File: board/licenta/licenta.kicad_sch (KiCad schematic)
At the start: 70 parts, among them IC1 SAMACSYS_PARTS_NCP186BMX330TAG, IC3 SAMACSYS_PARTS_BMI085, J1 SAMACSYS_PARTS_USB4110-GF-A, J2 SAMACSYS_PARTS_112A-TAAR-R03_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, J3 Conn_01x07, Q1 ESP32_WROVER_SPARKFUN-DISCRET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, Q2 2N7002, SW1 SELECT, SW2 UP, SW3 DOWN, SW4 RESET, SW5 DOWN, U1 ESP32-C3-MINI-1, U2 ESP32_WROVER_SPARKFUN-IC-POWE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, U3 DRV2605LDGS, U4 GC9A01_IPS_display_SPI, U5 A1027, U6 TPS3831, U7 ESP32-S3-MINI-1

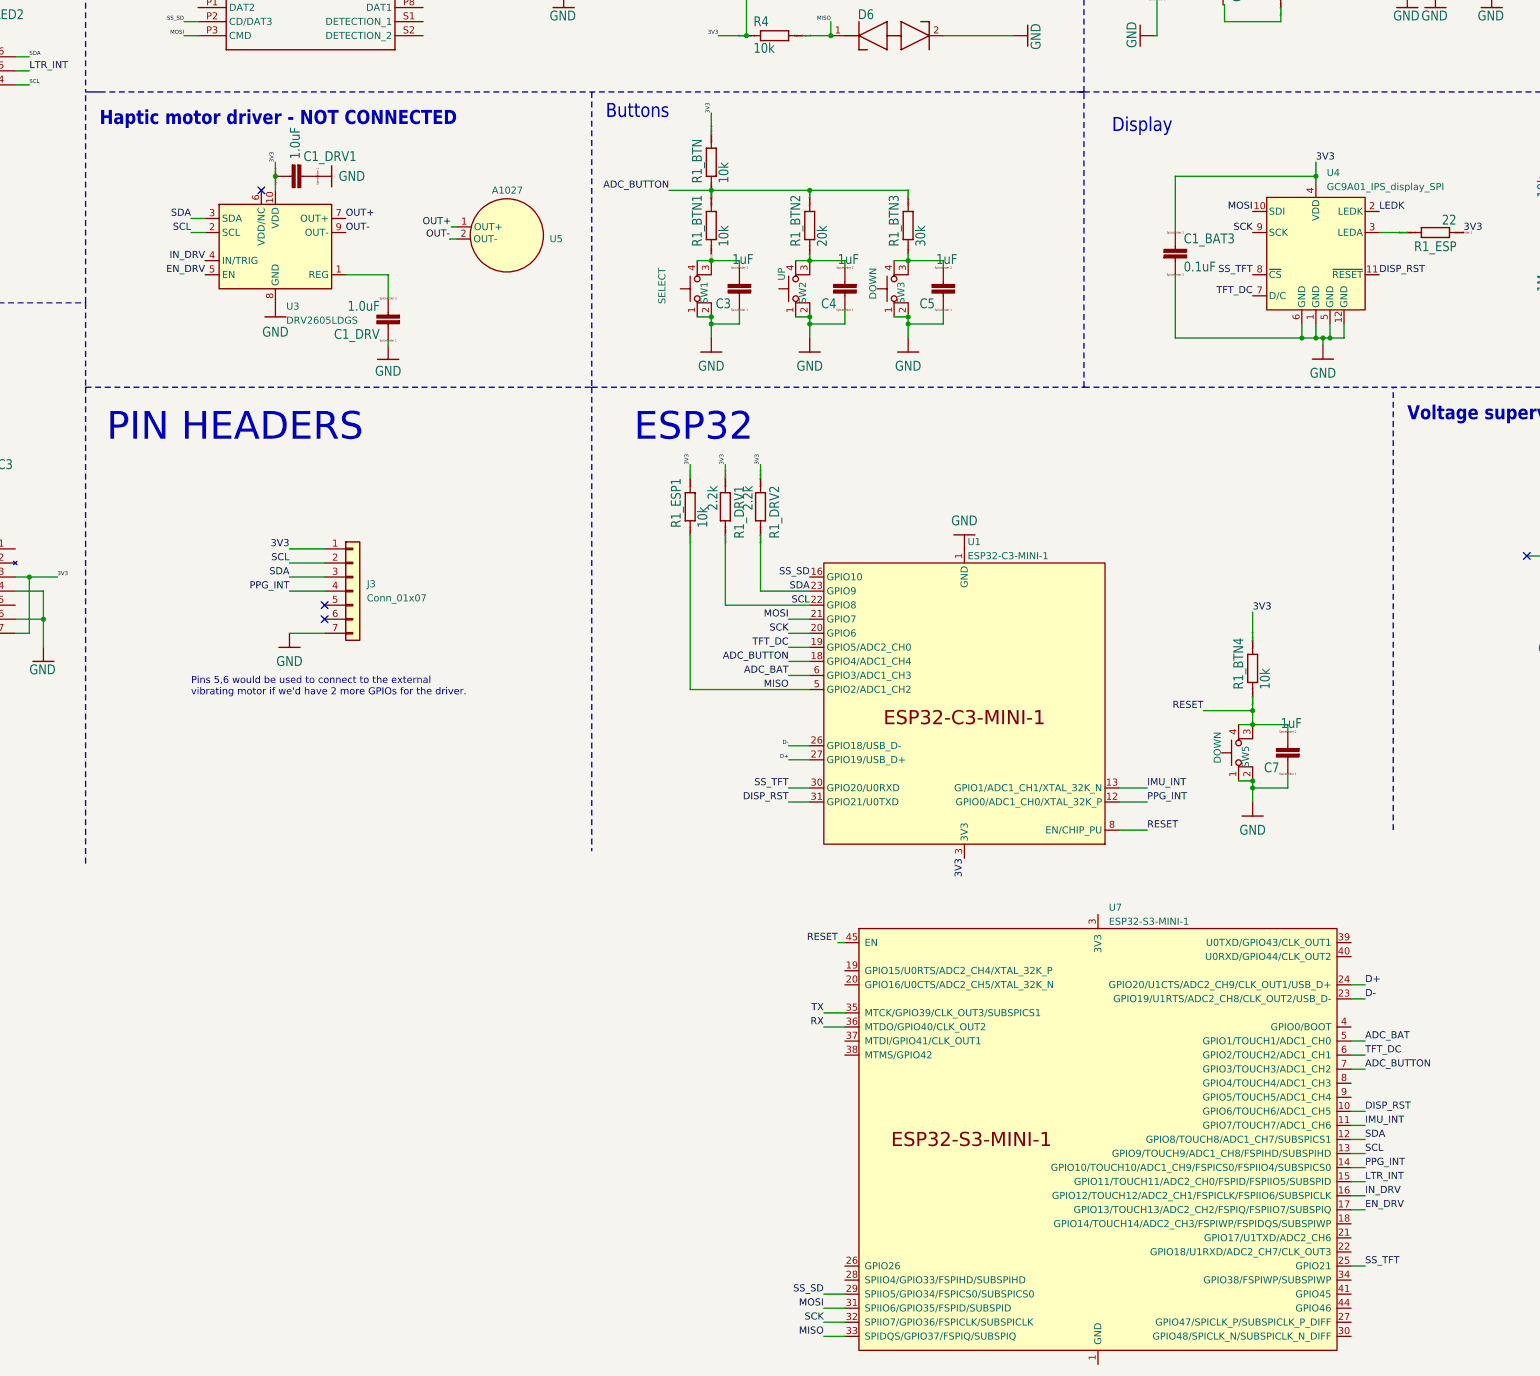
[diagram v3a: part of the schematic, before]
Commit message: board: Modify schematic to use ESP32 S3
Connect the haptic motor driver to the uC, add labels to pinheaders for A1027
and connect the buttons to different pins.
Delete ESP32 C3 mini from schematic.
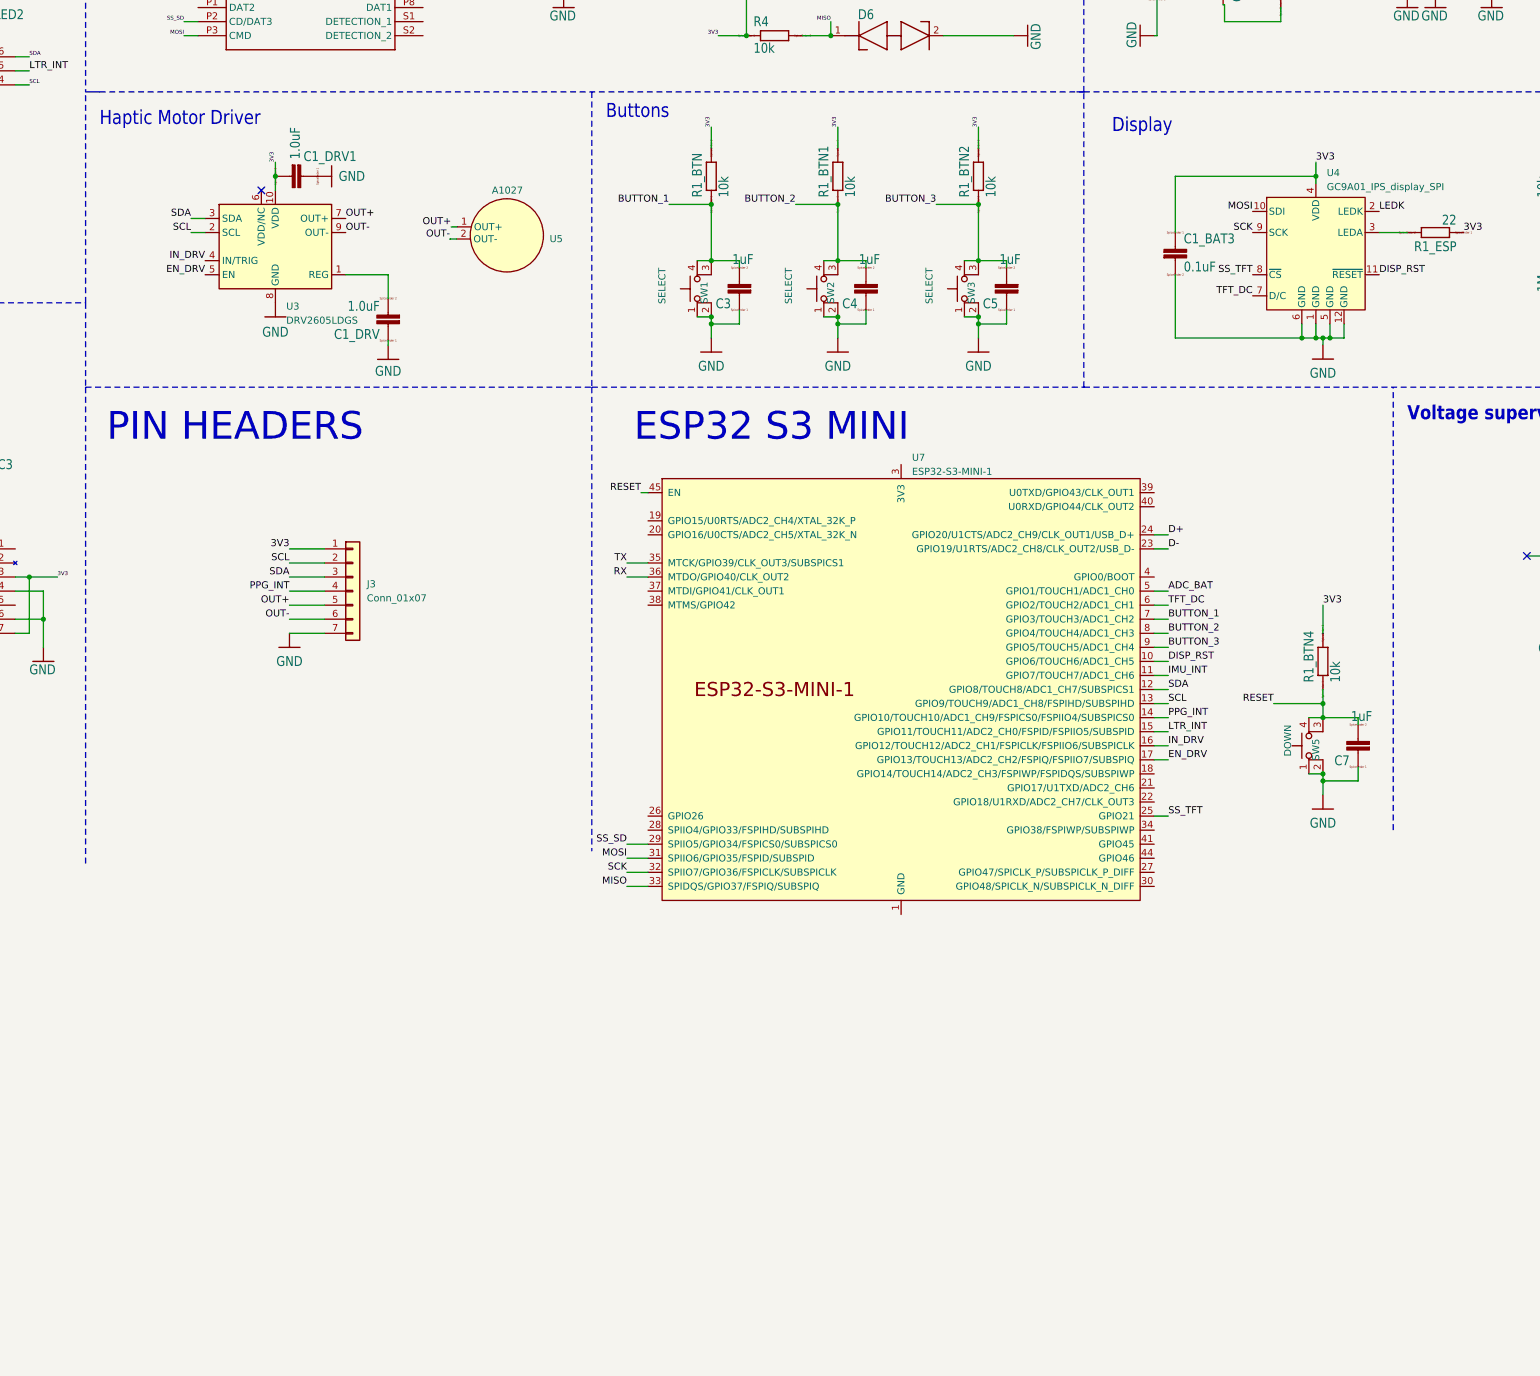
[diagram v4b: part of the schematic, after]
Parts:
- removed R1_BTN3: 30k, mini_iot:ESP32_WROVER_EAGLE-LTSPICE_R0402, symbol mini_iot-eagle-import:ESP32_WROVER_EAGLE-LTSPICE_RR0402
- removed R1_DRV1, R1_DRV2: 2.2k, mini_iot:ESP32_WROVER_EAGLE-LTSPICE_R0402, symbol mini_iot-eagle-import:ESP32_WROVER_EAGLE-LTSPICE_RR0402
- removed R1_ESP1: 10k, mini_iot:ESP32_WROVER_EAGLE-LTSPICE_R0402, symbol mini_iot-eagle-import:ESP32_WROVER_EAGLE-LTSPICE_RR0402
- removed U1: ESP32-C3-MINI-1, PCM_Espressif:ESP32-C3-MINI-1, symbol PCM_Espressif:ESP32-C3-MINI-1
- R1_BTN2: value 20k -> 10k
- SW2: value UP -> SELECT
- SW3: value DOWN -> SELECT
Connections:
- net 3V3: now also R1_BTN1.2, R1_BTN2.2
- net OUT+: now also J3.5 (Pin_5)
- net OUT-: now also J3.6 (Pin_6)
- net BUTTON_1: now reaches C3.2, SW1.3 (K), SW1.4 (A)
- net BUTTON_1: now also R1_BTN.1, U7.7 (GPIO3/TOUCH3/ADC1_CH2)
- net BUTTON_3: now reaches C5.2, SW3.3 (K), SW3.4 (A)
- net BUTTON_3: now also R1_BTN2.1, U7.9 (GPIO5/TOUCH5/ADC1_CH4)
- net BUTTON_2: now reaches C4.2, SW2.3 (K), SW2.4 (A)
- net BUTTON_2: now also R1_BTN1.1, U7.8 (GPIO4/TOUCH4/ADC1_CH3); no longer R1_BTN2.1
- removed net ADC_BUTTON: R1_BTN.1, R1_BTN1.2, R1_BTN2.2, U7.7 (GPIO3/TOUCH3/ADC1_CH2)
- no-connect marks 5 -> 3
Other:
- note added: "ESP32 S3 MINI"
- note added: "Haptic Motor Driver"
- note removed: "ESP32"
- note removed: "Haptic motor driver - NOT CONNECTED"
- note removed: "Pins 5,6 would be used to connect to the external vibrating motor if we'd have 2 more GPIOs for the driver."
- moved on the sheet: C7, R1_BTN, R1_BTN4, SW5, U7

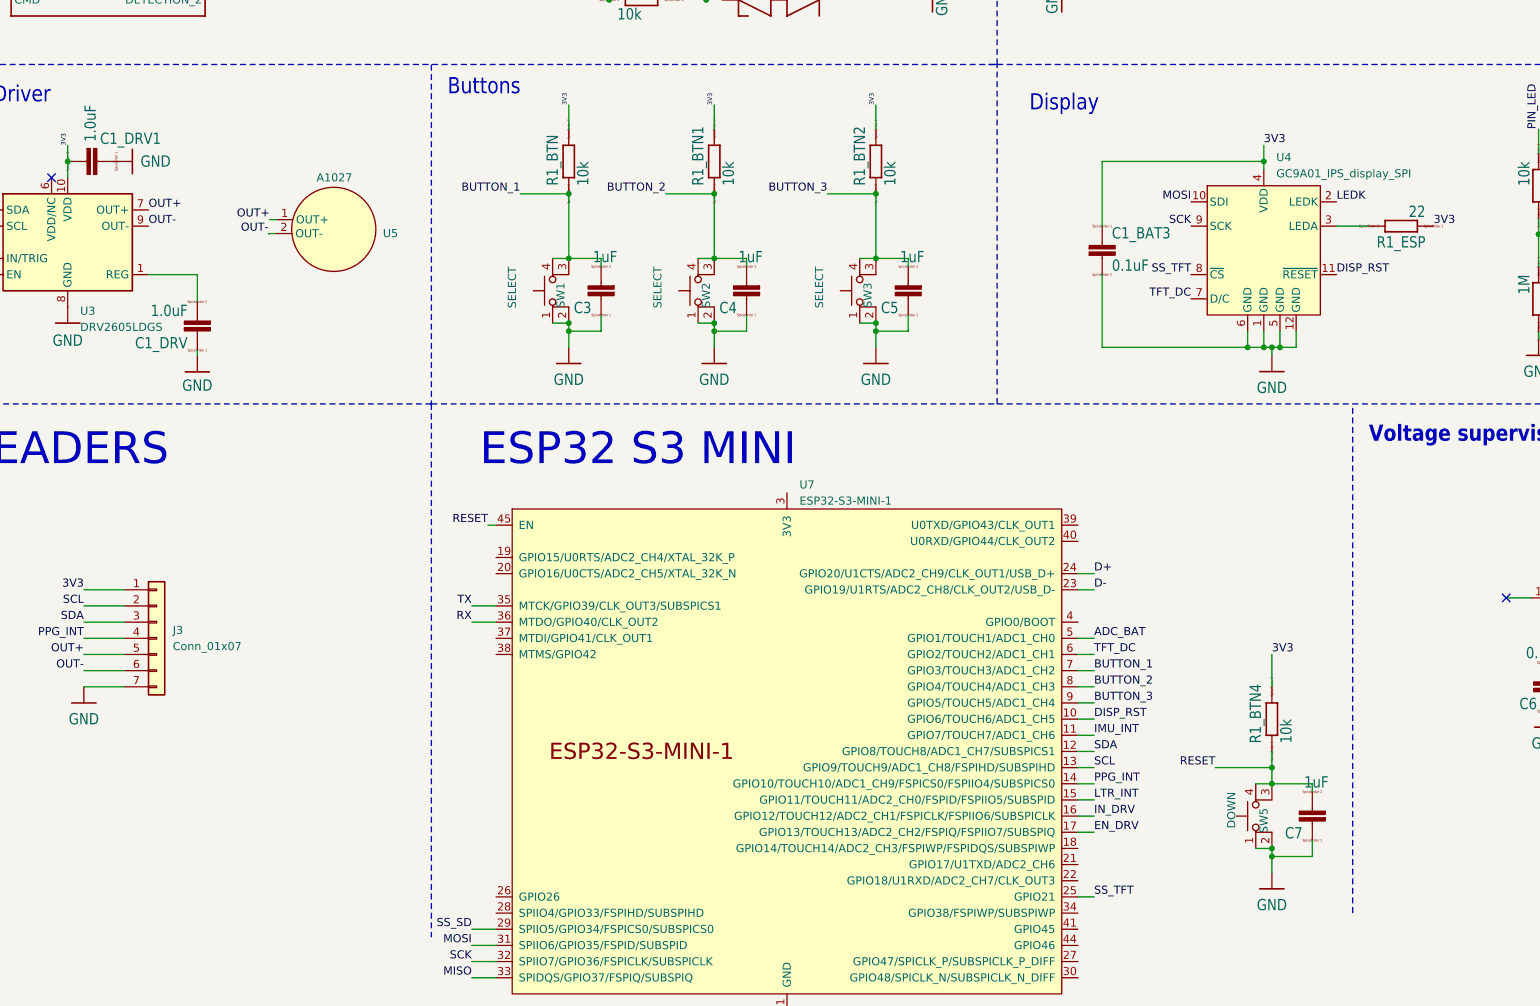
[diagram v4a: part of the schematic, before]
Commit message: board: Add PCB draft
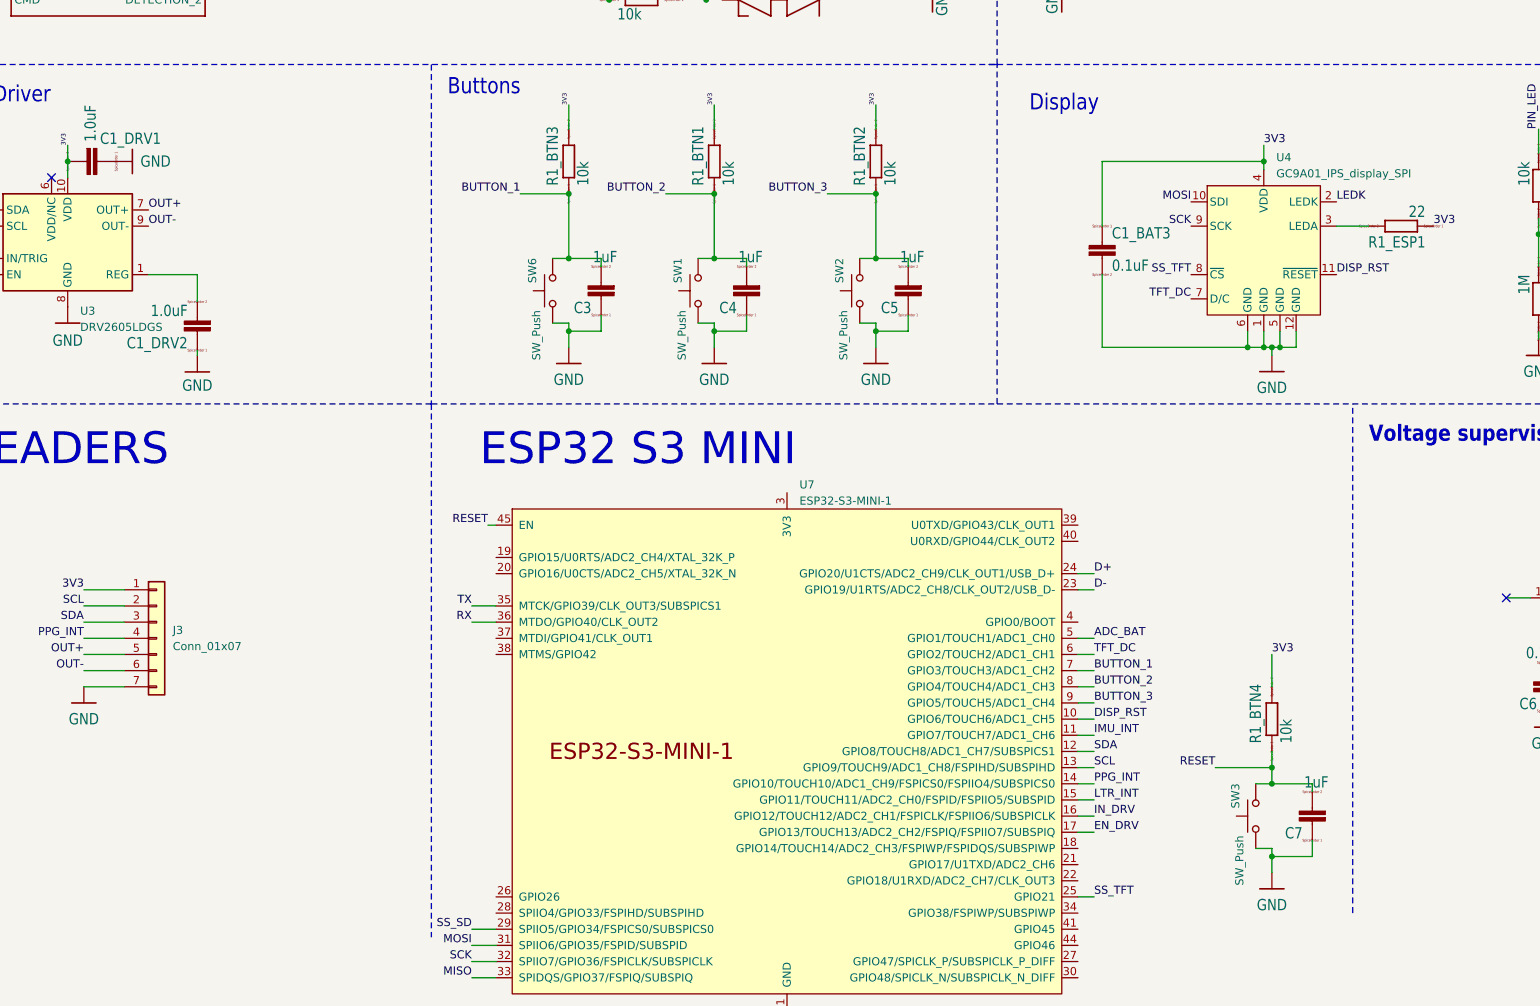
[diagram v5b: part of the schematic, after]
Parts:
- removed SW1, SW2, SW3: SELECT, Button_Switch_THT:SW_PUSH_LCD_E3_SAxxxx, symbol Switch:SW_MEC_5E
- removed SW5: DOWN, Button_Switch_THT:SW_PUSH_LCD_E3_SAxxxx, symbol Switch:SW_MEC_5E
- removed U5: A1027, symbol licenta:A1027
- added SW1, SW2, SW3, SW6: SW_Push, open-Smartwatch:button_side_smd, symbol Switch:SW_Push
- J3: footprint (none) -> Connector_PinHeader_2.54mm:PinHeader_1x07_P2.54mm_Vertical
- renumbered C1_DRV to C1_DRV2, R1_BTN to R1_BTN3, R1_ESP to R1_ESP1
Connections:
- net BUTTON_1: now also SW6.2
- net BUTTON_2: now also SW1.2
- net BUTTON_3: now also SW2.2
- net GND: now also SW1.1, SW2.1, SW3.1, SW6.1
- net RESET: now also SW3.2

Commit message: Update schematics
Delete unused components such as LTR and voltage supervisor.
Replace pinheaders with test pads
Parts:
- removed C1_SENSOR0: 100nF, mini_iot:ESP32_WROVER_EAGLE-LTSPICE_C0402, symbol mini_iot-eagle-import:ESP32_WROVER_EAGLE-LTSPICE_CC0402
- removed C6: 0.1uF, mini_iot:ESP32_WROVER_EAGLE-LTSPICE_C0402, symbol mini_iot-eagle-import:ESP32_WROVER_EAGLE-LTSPICE_CC0402
- removed J3: Conn_01x07, Connector_PinHeader_2.54mm:PinHeader_1x07_P2.54mm_Vertical, symbol Connector_Generic:Conn_01x07
- removed LED2: ESP32_WROVER_SAMACSYS_PARTS_LTR-303ALS-01, mini_iot:ESP32_WROVER_SAMACSYS_PARTS_LTR303ALS01, symbol mini_iot-eagle-import:ESP32_WROVER_SAMACSYS_PARTS_LTR-303ALS-01
- removed SW4: RESET, Button_Switch_THT:SW_PUSH_LCD_E3_SAxxxx, symbol Switch:SW_MEC_5E
- removed U6: TPS3831, Package_SON:Texas_X2SON-4_1x1mm_P0.65mm, symbol Power_Supervisor:TPS3831
- added TP1, TP2, TP3, TP4, TP5, TP6, TP7: TestPoint, TestPoint:TestPoint_Pad_D2.0mm, symbol Connector:TestPoint
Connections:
- net 3V3: now also TP1.1
- net GND: now also TP7.1
- net OUT+: now also TP5.1
- net OUT-: now also TP6.1
- net PPG_INT: now also TP4.1
- net SCL: now also TP2.1
- net SDA: now also TP3.1
- no-connect marks 3 -> 1
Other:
- note added: "TEST POINTS"
- note removed: "Ambient Light Sensor LTR303"
- note removed: "PIN HEADERS"
- note removed: "Voltage supervisor - NOT CONNECTED"
